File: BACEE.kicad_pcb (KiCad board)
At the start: 2 copper layers, 42.7 x 24.4 mm, 20 parts, among them J2 I2C connector, J3 Digital pins, J4 Serial connector, J5 ICSP, U1 24LC1025, U2 DS1337S+, U3 24LC1025, U4 ATMEGA328P-AU, Y1 Crystal 32768 kHz, Y2 Crystal 16MHz

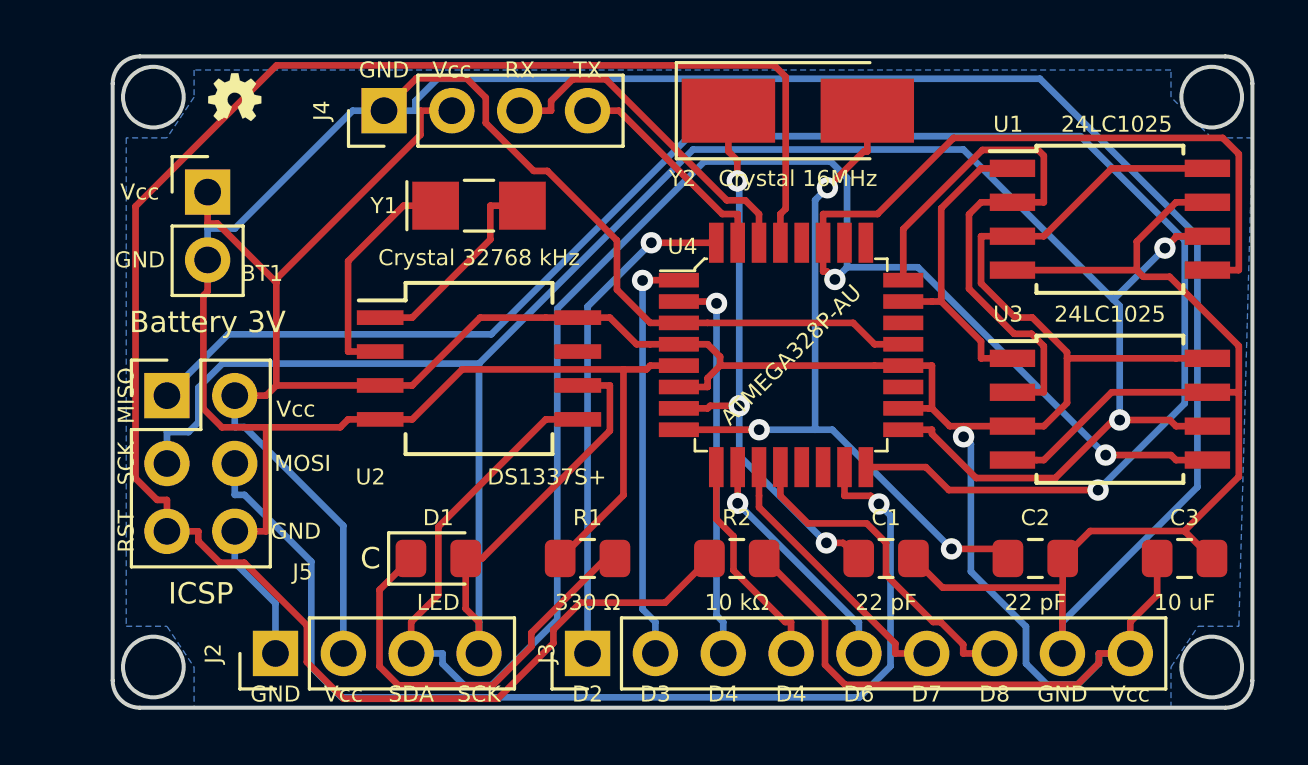
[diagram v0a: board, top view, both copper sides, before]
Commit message: Fixed layout wiring to implement the fix in EEPROM addressing.
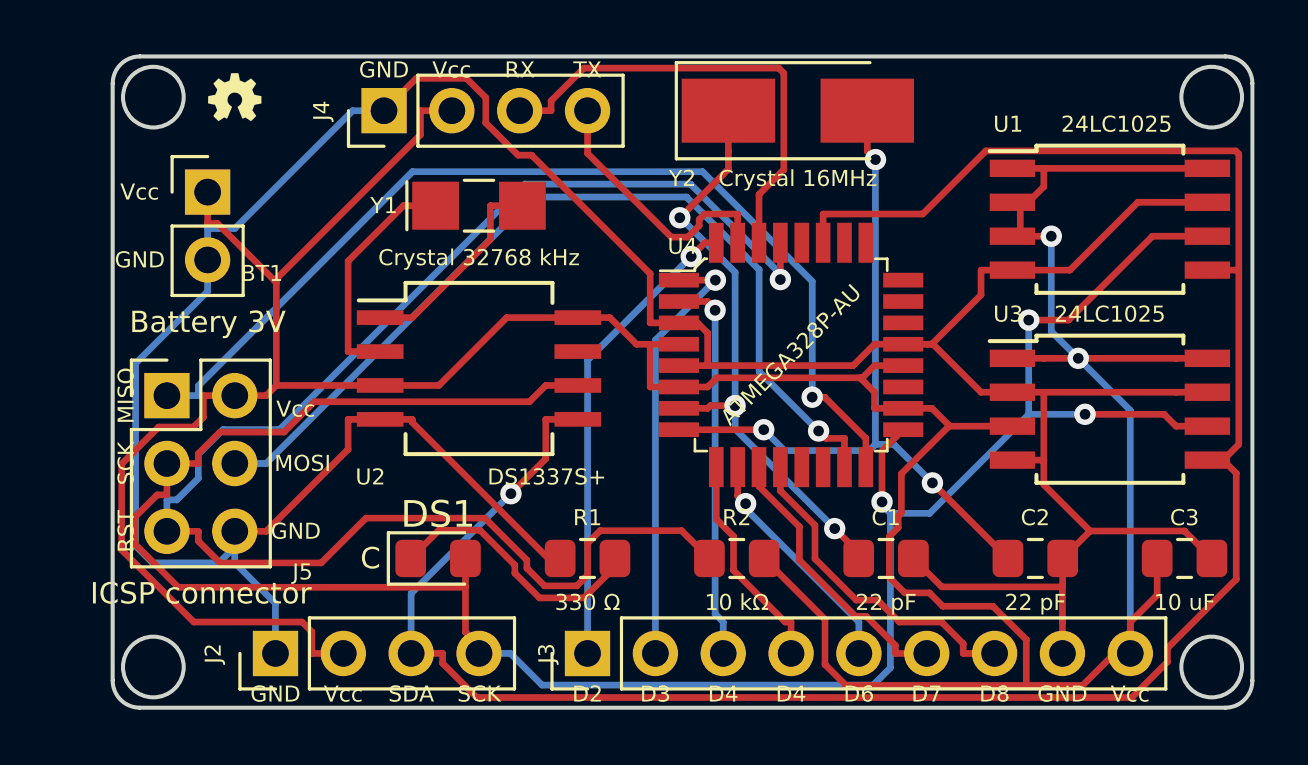
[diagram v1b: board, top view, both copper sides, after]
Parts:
- removed D1: LED, LED_SMD:LED_0805_2012Metric_Pad1.15x1.40mm_HandSolder
- added DS1: LED, LED_SMD:LED_0805_2012Metric_Pad1.15x1.40mm_HandSolder, F.Cu at (107.2, 109.7)
- J5: value ICSP -> ICSP connector
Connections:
- BT1 pad 2: GND -> GNDPWR
- C1 pad 2: GND -> GNDPWR
- C2 pad 2: GND -> GNDPWR
- C3 pad 2: GND -> GNDPWR
- J2 pad 1: GND -> GNDPWR
- J3 pad 8: GND -> GNDPWR
- J4 pad 1: GND -> GNDPWR
- J5 pad 6: GND -> GNDPWR
- R1 pad 1: GND -> GNDPWR
- U1 pad 1: /ADDS1 -> /Vcc
- U1 pad 2: /ADDS2 -> /Vcc
- U1 pad 4: GND -> GNDPWR
- U1 pad 7: GND -> GNDPWR
- U2 pad 4: GND -> GNDPWR
- U3 pad 1: /ADDS1 -> /Vcc
- U3 pad 2: /ADDS2 -> GNDPWR
- U3 pad 4: GND -> GNDPWR
- U3 pad 7: GND -> GNDPWR
- U4 pad 21: GND -> GNDPWR
- U4 pad 3: GND -> GNDPWR
- U4 pad 5: GND -> GNDPWR
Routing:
- net GND: track 176.9 -> 0.00 mm
- net GNDPWR: track 0.00 -> 124.1 mm
- net /MISO: track 63.5 -> 37.6 mm
- net /ADDS2: track 22.6 -> 0.00 mm
- net /Vcc: track 127.4 -> 146.2 mm, vias 1 -> 2
- net /RESET: track 72.3 -> 57.5 mm, vias 0 -> 1
- net /ADDS1: track 12.1 -> 0.00 mm
- net /SDA: track 90.0 -> 81.8 mm, vias 2 -> 1
- net /MOSI: track 40.4 -> 34.0 mm
- net Net-(DS1-Pad1): track 15.9 -> 10.1 mm
- net /RX: track 12.8 -> 17.6 mm
- net /SCK: track 91.3 -> 88.0 mm, vias 2 -> 3
- net /TX: track 8.30 -> 10.1 mm
- net /D2: track 18.8 -> 17.6 mm
- net Net-(C1-Pad1): track 21.5 -> 22.5 mm
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- removed copper zone on B.Cu, net GND

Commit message: Gerbers for version 1.1.
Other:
- board text added: "Arduino clone with - 2Mbit EEPROM - Clock & calendar - I2C, SPI & GPIOs Version 1.1"
- board text removed: "Arduino clone with - 2Mbit EEPROM - Clock & calendar - I2C, SPI & GPIOs"
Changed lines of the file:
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@@
       (effects (font (size 0.6 0.6) (thickness 0.15)))
     )
-    (fp_text value "ICSP connector" (at 1.27 7.41) (layer F.SilkS)
+    (fp_text value "ICSP connector" (at 2.794 7.62) (layer F.SilkS)
       (effects (font (size 0.8 0.8) (thickness 0.15)))
     )
@@
     (arrow2b (pts (xy 94.996 89.154) (xy 96.122504 88.567579)))
   )
-  (gr_text "Designed by Peter in Berowra\n" (at 136.652 109.982) (layer B.SilkS)
+  (gr_text "Designed by Peter in Berowra\n" (at 136.652 110.744) (layer B.SilkS)
     (effects (font (size 1 1) (thickness 0.25) italic) (justify left mirror))
   )
-  (gr_text "Arduino clone with\n- 2Mbit EEPROM\n- Clock & calendar\n- I2C, SPI & GPIOs" (at 136.906 105.156) (layer B.SilkS)
+  (gr_text "Arduino clone with\n- 2Mbit EEPROM\n- Clock & calendar\n- I2C, SPI & GPIOs\nVersion 1.1" (at 136.906 105.156) (layer B.SilkS)
     (effects (font (size 1 1) (thickness 0.25)) (justify left mirror))
   )

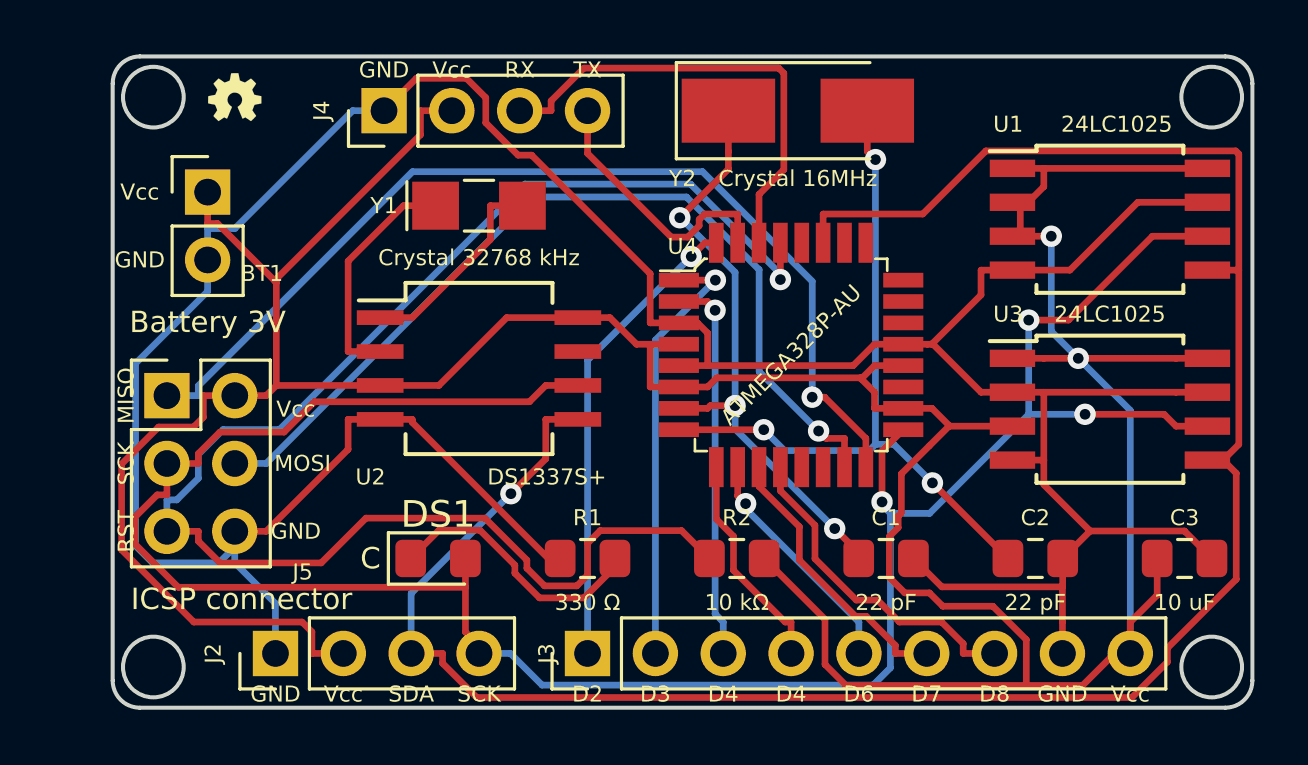
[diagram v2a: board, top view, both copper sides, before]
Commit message: Corrected EEPROM addressing error in the four layer board.
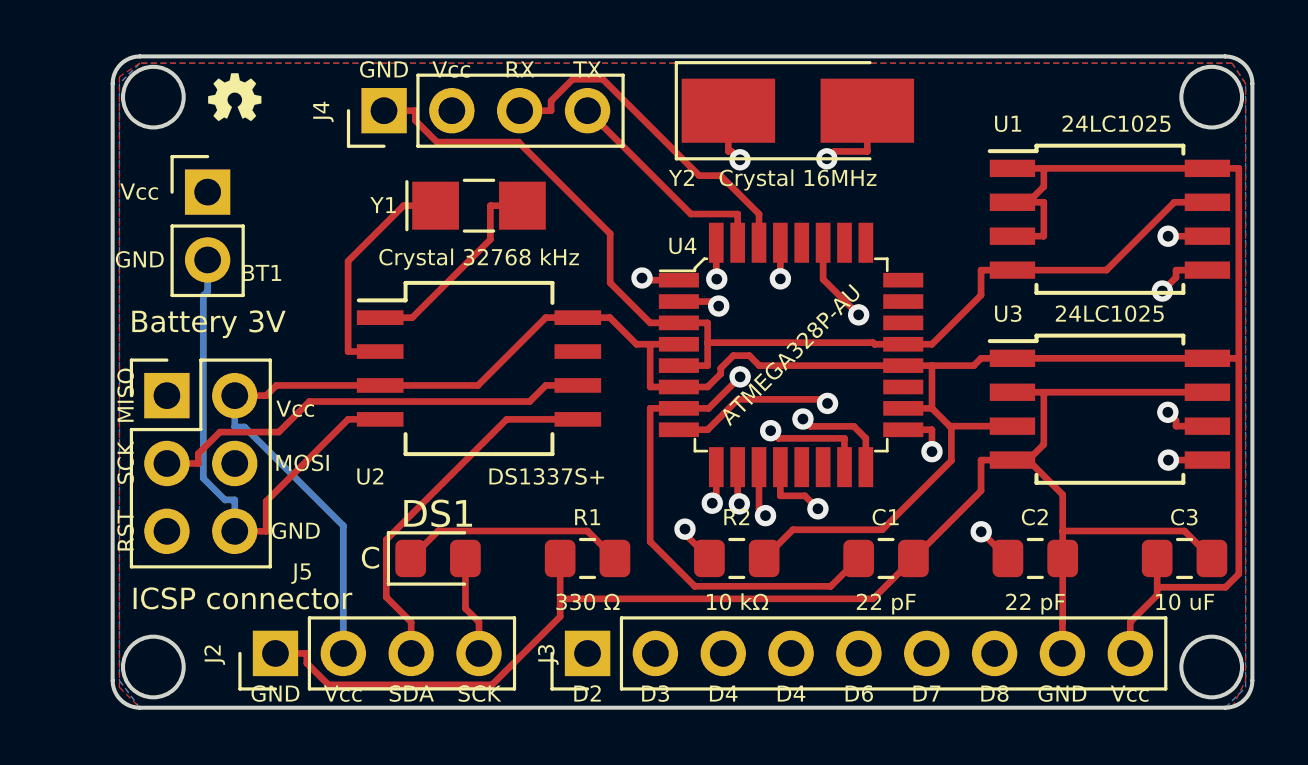
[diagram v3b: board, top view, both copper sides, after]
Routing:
- net /RESET: track 57.5 -> 34.2 mm, vias 1 -> 2
- net /Vcc: track 146.2 -> 125.0 mm, vias 2 -> 0
- net /SDA: track 81.8 -> 63.5 mm, vias 1 -> 3
- net /SCK: track 88.0 -> 77.4 mm
- net /MOSI: track 34.0 -> 24.5 mm
- net GNDPWR: track 124.1 -> 133.3 mm
- net /MISO: track 37.6 -> 28.6 mm
- net /D3: track 16.3 -> 22.6 mm
- net Net-(C1-Pad1): track 22.5 -> 28.0 mm, vias 3 -> 2
- net /RX: track 17.6 -> 12.8 mm
- net /D4: track 14.5 -> 16.3 mm
- net /TX: track 10.1 -> 8.30 mm
- net Net-(DS1-Pad1): track 10.1 -> 8.50 mm
- net /D8: track 12.4 -> 11.8 mm, vias 0 -> 1
- net /D7: track 10.5 -> 10.4 mm, vias 0 -> 1
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- added copper zone on F.Cu, net /Vcc
- added copper zone on B.Cu, net GNDPWR
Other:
- copper layers 2 -> 4
- board text added: "Arduino clone with - 2Mbit EEPROM - Clock & calendar - I2C, SPI & GPIOs Version 1.1 - Four layers"
- board text removed: "Arduino clone with - 2Mbit EEPROM - Clock & calendar - I2C, SPI & GPIOs Version 1.1"
